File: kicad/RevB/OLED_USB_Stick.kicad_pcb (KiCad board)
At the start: 2 copper layers, 62.5 x 14.7 mm, 27 parts, among them J1 USB_A, J3 Conn_01x04, SW1 SW_SPDT, SW2 SW_SPST, U1 FT232RL, U2 SE8233X2, U3 STM32F051K4Tx

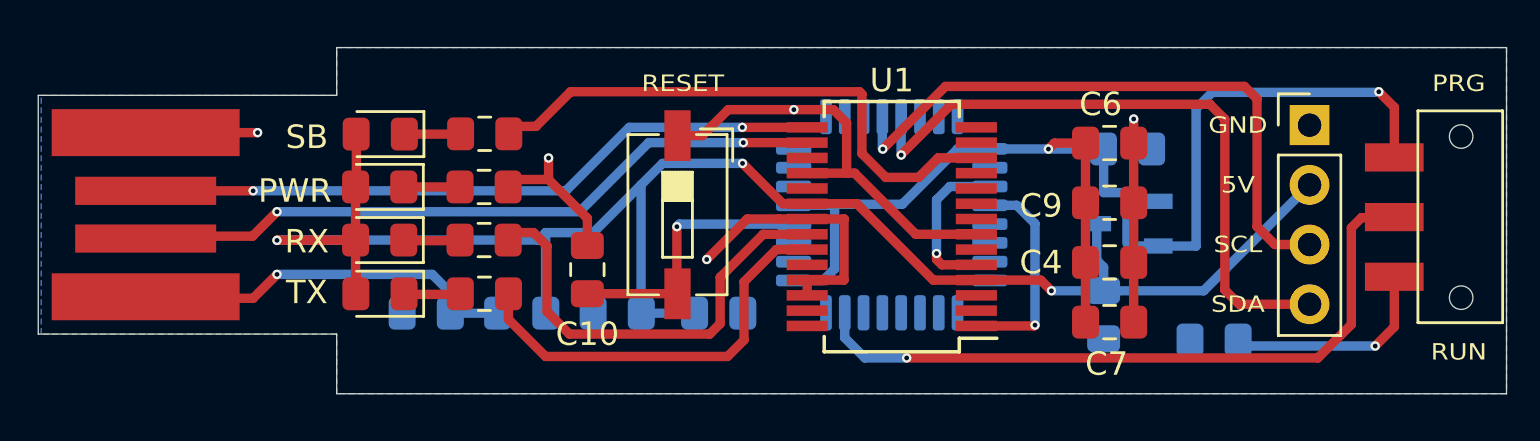
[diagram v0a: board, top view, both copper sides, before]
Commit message: updated revb hw
- Added pull up resistors to i2C bus (allows direct connection to mcu from oled port)
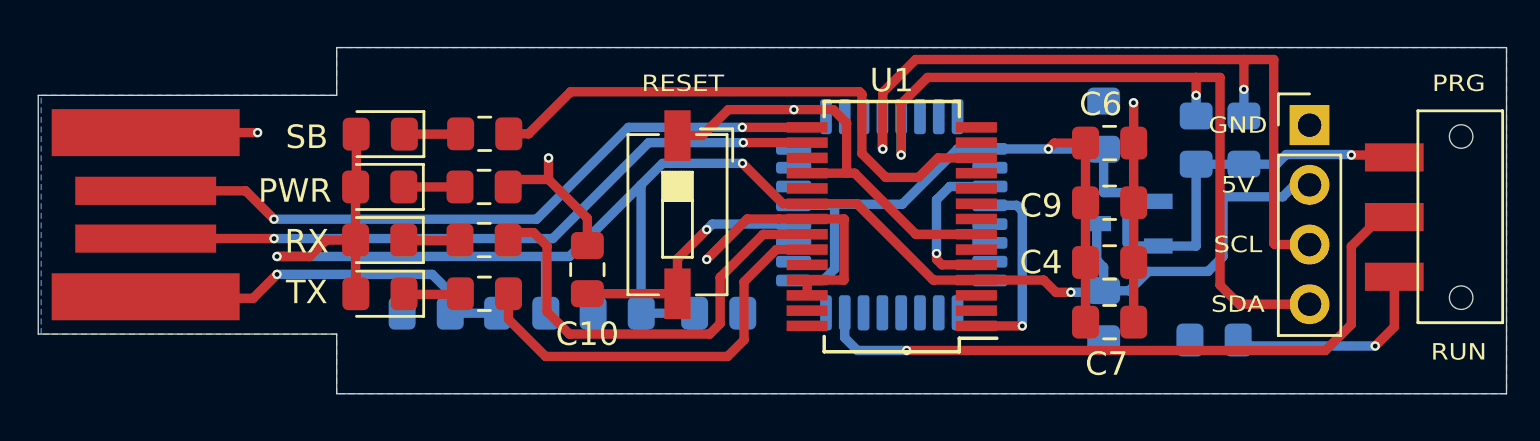
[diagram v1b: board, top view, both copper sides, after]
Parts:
- added R6: 10K, Resistor_SMD:R_0805_2012Metric_Pad1.15x1.40mm_HandSolder, B.Cu at (176.3, 75.6)
- added R7: 10K, Resistor_SMD:R_0805_2012Metric_Pad1.15x1.40mm_HandSolder, B.Cu at (174.2, 75.6)
- moved C8 1.44 mm to (170.3, 74.9), turned to 90 degrees
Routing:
- net /MCU/I2C_SCL: track 26.6 -> 32.9 mm, vias 1 -> 2
- net +3V3: track 53.6 -> 48.8 mm
- net /MCU/I2C_SDA: track 27.7 -> 32.5 mm, vias 1 -> 2
- net Net-(J1-Pad3): track 29.3 -> 30.3 mm
- net +5V: track 74.9 -> 75.8 mm
- net Net-(C10-Pad1): track 11.7 -> 10.9 mm
- net /MCU/USART_RX: track 9.07 -> 8.33 mm
- net Net-(SW1-Pad2): track 29.1 -> 28.4 mm
- net GNDS: track 49.2 -> 49.9 mm
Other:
- board text added: "OLED USB Stick RevB 3920"

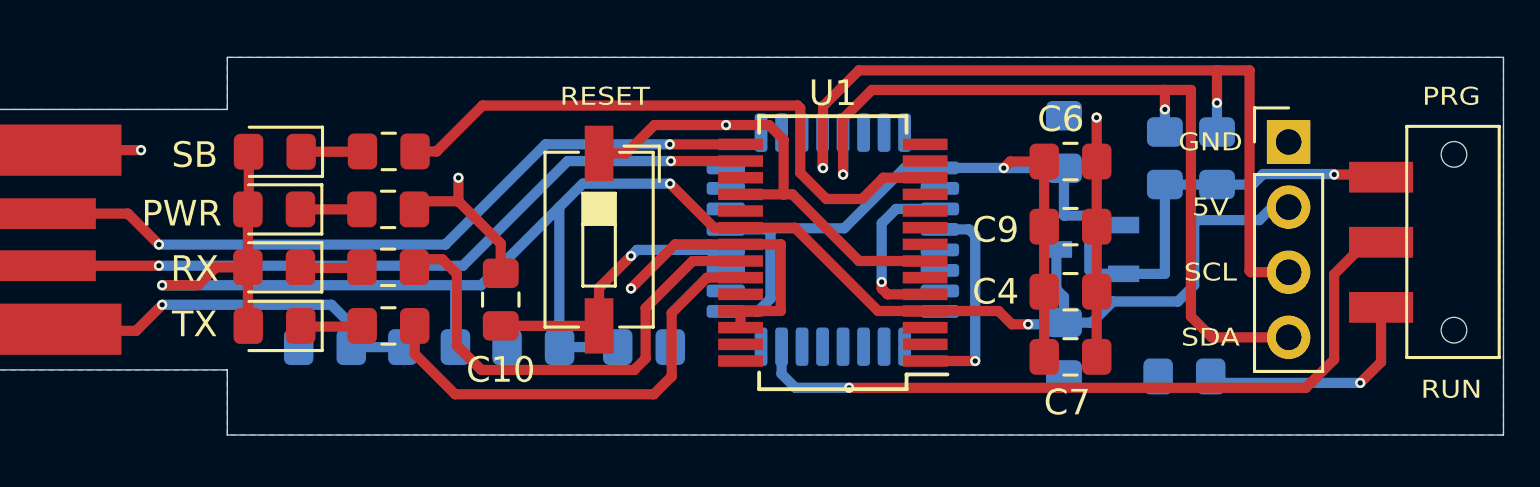
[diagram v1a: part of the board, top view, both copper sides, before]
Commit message: updated hw
- corrected i2c pins
- changed reset btn to horizontal mount
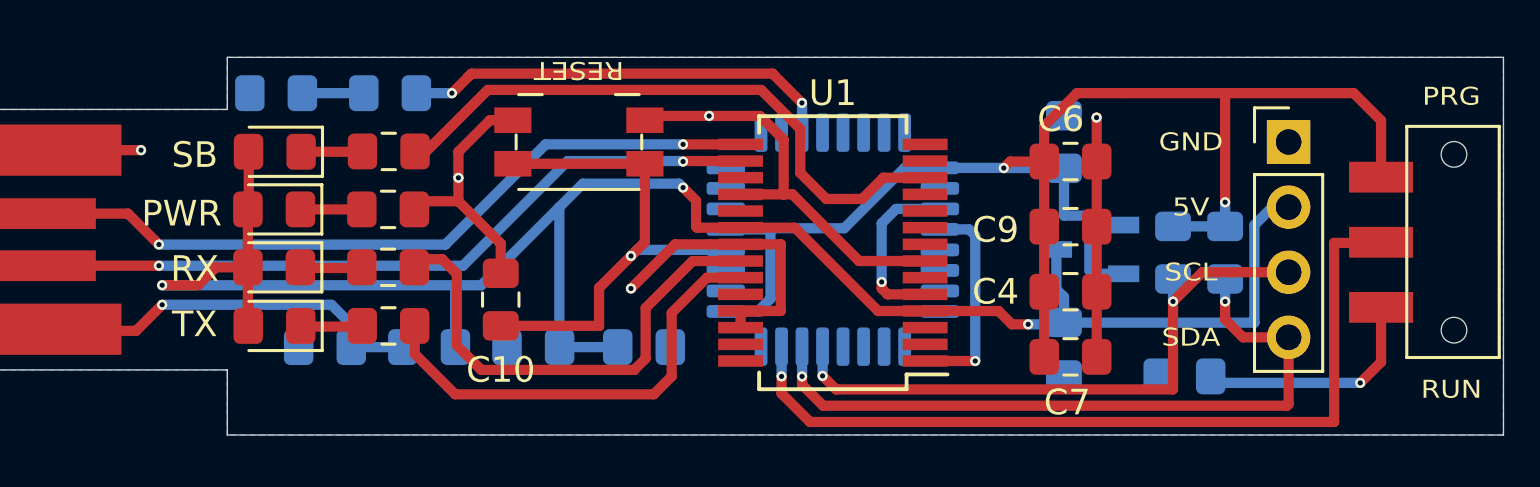
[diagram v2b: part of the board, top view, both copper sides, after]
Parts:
- added D5: LED, LED_SMD:LED_0805_2012Metric_Pad1.15x1.40mm_HandSolder, B.Cu at (144.0, 73.0)
- added R8: 1K, Resistor_SMD:R_0805_2012Metric_Pad1.15x1.40mm_HandSolder, B.Cu at (139.6, 73.0)
- SW2: footprint Button_Switch_SMD:SW_DIP_SPSTx01_Slide_6.7x4.1mm_W6.73mm_P2.54mm_LowProfile_JPin -> Button_Switch_SMD:Panasonic_EVQPUK_EVQPUB
- moved R7 4.37 mm to (176.6, 79.2), turned to 270 degrees
- moved R6 4.06 mm to (174.6, 79.2), turned to 270 degrees
- moved SW2 3.89 mm to (151.4, 74.9), turned to 0 degrees
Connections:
- net /MCU/USART_RX renamed /USB_TO_RS232/FT232_TX
- net /MCU/USART_TX renamed /USB_TO_RS232/FT232_RX
- U3 pad 12: /MCU/I2C_SCL -> Net-(U3-Pad12)
- U3 pad 13: /MCU/I2C_SDA -> Net-(U3-Pad13)
- U3 pad 29: Net-(U3-Pad29) -> /MCU/I2C_SCL
- U3 pad 30: Net-(U3-Pad30) -> /MCU/I2C_SDA
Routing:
- net Net-(D5-Pad2): track 0.00 -> 17.0 mm, vias 0 -> 2
- net +3V3: track 48.8 -> 60.0 mm
- net Net-(C10-Pad1): track 10.9 -> 19.8 mm
- net /MCU/I2C_SCL: track 32.9 -> 24.3 mm
- net /MCU/I2C_SDA: track 32.5 -> 27.8 mm
- net Net-(SW1-Pad2): track 28.4 -> 32.7 mm
- net Net-(D5-Pad1): track 0.00 -> 2.39 mm
- net GNDS: track 49.9 -> 51.6 mm
- net +5V: track 75.8 -> 77.2 mm

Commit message: update readme
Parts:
- moved C10 92.5 mm to (65.5, 39.9)
- moved C4 92.5 mm to (87.8, 39.6)
- moved D1 92.5 mm to (56.7, 41.0)
- moved D2 92.5 mm to (56.7, 38.7)
- moved D3 92.5 mm to (56.7, 34.2)
- moved D5 92.5 mm to (61.2, 31.9)
- moved R1 92.5 mm to (61.2, 41.0)
- moved R2 92.5 mm to (61.1, 38.7)
- moved R6 92.5 mm to (91.8, 38.1)
- moved R7 92.5 mm to (93.8, 38.1)
- moved R8 92.5 mm to (56.8, 31.9)
- moved C1 92.5 mm to (58.7, 41.8)
- moved C2 92.5 mm to (66.8, 41.8)
- moved C3 92.5 mm to (71.1, 41.8)
- moved C5 92.5 mm to (87.5, 41.8)
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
